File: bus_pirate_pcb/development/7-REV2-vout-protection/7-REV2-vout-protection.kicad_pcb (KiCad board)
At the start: 4 copper layers, 80 x 80.2 mm, 264 parts, among them J201 Conn_01x03, J202 TYPE-C-31-M-12, J301 Conn_01x10, J302 Conn_01x09, Q1 2N7002KT, Q2 2N7002KT, Q3 PMXB56EN, Q4 PMXB56EN, Q5 2N7002KT, Q6 2N7002KT, Q601 MMDT3906DW, Q602 BC2301T 2.8A, SW101 TS3425BA 098 2.5H 250gf, SW102 TS3315A 250gf 025, U1 RP2350B, U10 GS358-FR, U102 W25Q128JVSIQ, U105 MT29F2G01ABAGDWB-IT:G, U11 GS358-FR, U117 LM393BIDSGR, U12 GS358-FR, U13 GS358-FR, U14 SP3002-04JTG, U15 SP3002-04JTG, U16 SP3002-04JTG, U17 TLV75801PDRV, U2 AiP74LVC8T245QE24.TR, U301 AiP74LVC1T45GC363.TR, U302 AiP74LVC1T45GC363.TR, U303 AiP74LVC1T45GC363.TR, U304 AiP74LVC1T45GC363.TR, U305 AiP74LVC1T45GC363.TR, U306 AiP74LVC1T45GC363.TR, U307 AiP74LVC1T45GC363.TR, U308 AiP74LVC1T45GC363.TR, U4 XL9555QF24, U401 ME6211A33PG-N, U402 CD4067, U403 AP2127K-ADJ, U5 GS358-FR, U503 74HCT245BQ, U6 TCA6416ARTWR, U601 GS321A-TR, U602 GSV331-TR, U7 TCA6416ARTWR, U8 APS6404L-3SQR-ZR, U9 GS358-FR, Y101 ABM8-272-T3

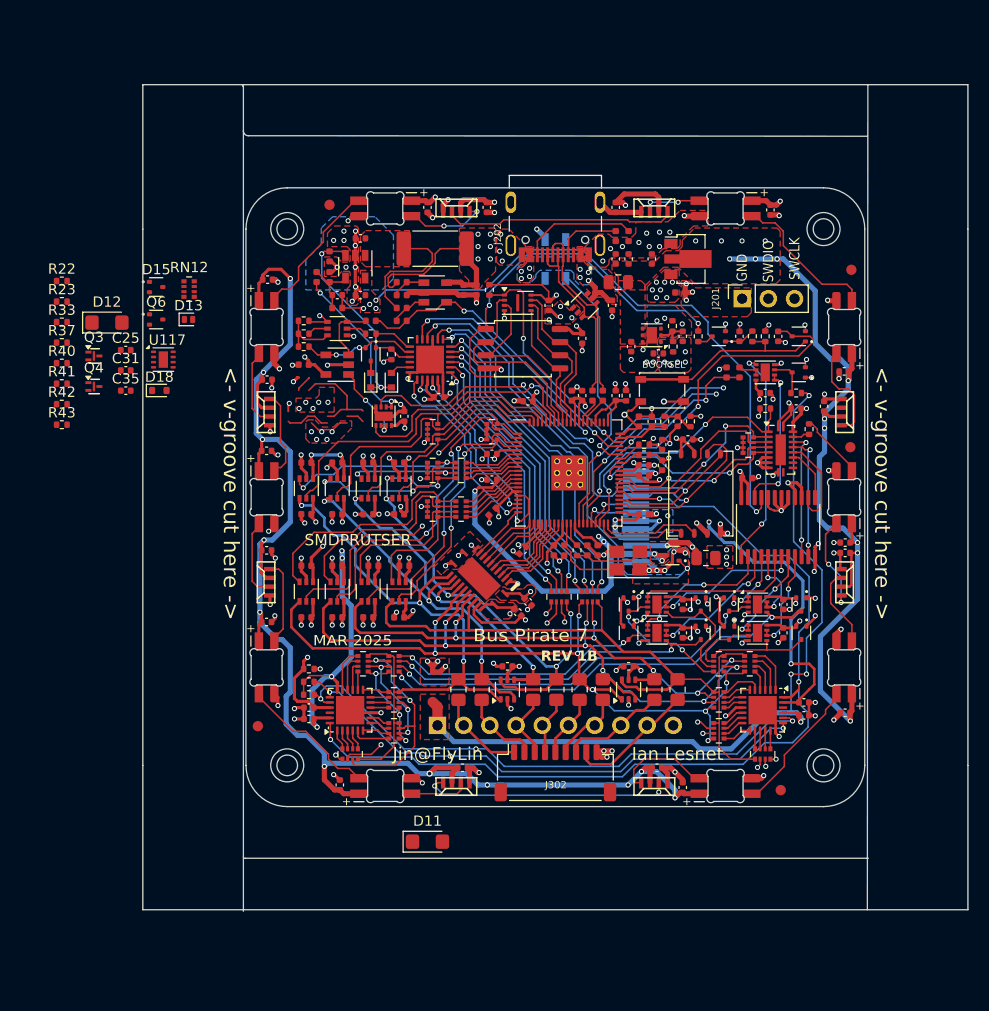
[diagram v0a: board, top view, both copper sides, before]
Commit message: BP 7R2 VOUT protection
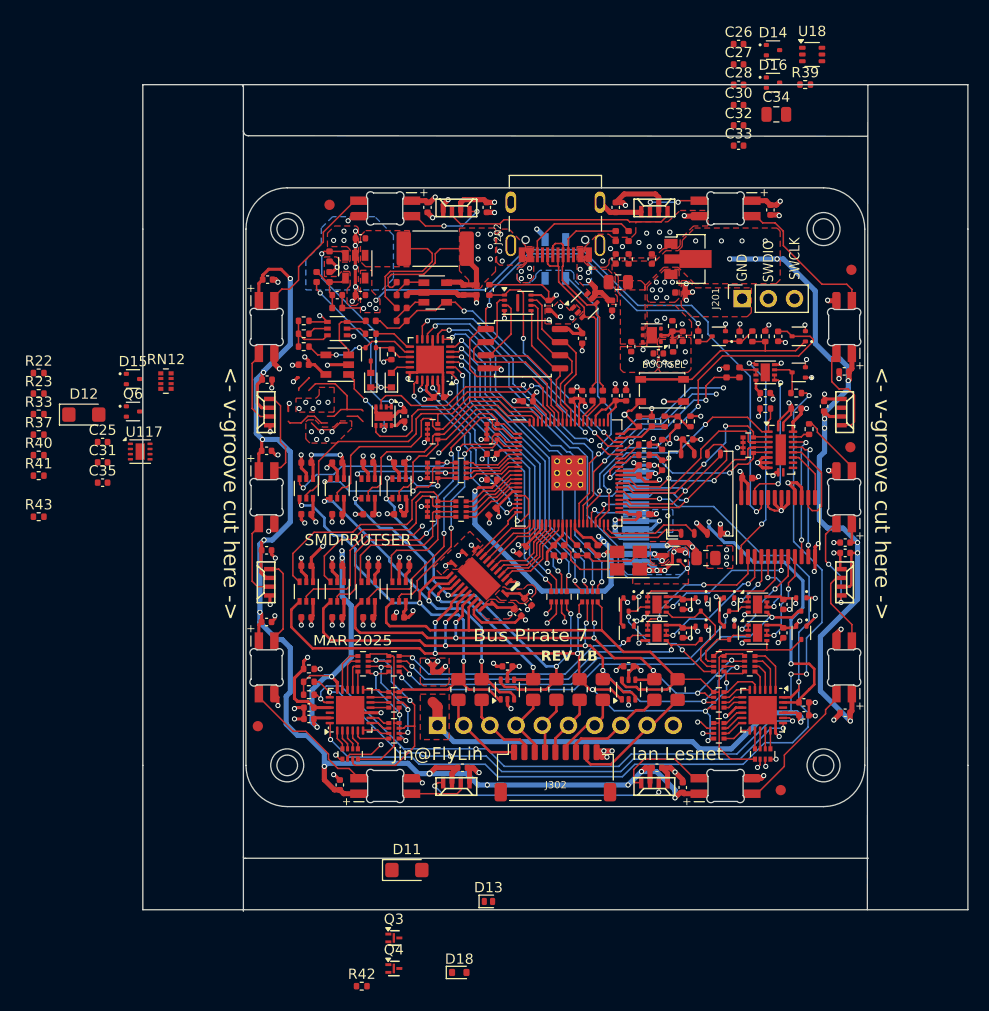
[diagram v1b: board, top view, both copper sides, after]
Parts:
- added C26: 120pF, Capacitor_SMD:C_0402_1005Metric, F.Cu at (147.7, 46.2)
- added C27: 10uF/6.3v, Capacitor_SMD:C_0402_1005Metric, F.Cu at (147.7, 48.1)
- added C28: 0.1uF, Capacitor_SMD:C_0402_1005Metric, F.Cu at (147.7, 50.1)
- added C30: 10uF/6.3v, Capacitor_SMD:C_0402_1005Metric, F.Cu at (147.7, 52.1)
- added C32: 0.1uF, Capacitor_SMD:C_0402_1005Metric, F.Cu at (147.7, 54.0)
- added C33: 10uF/6.3v, Capacitor_SMD:C_0402_1005Metric, F.Cu at (147.7, 56.0)
- added C34: 10uF/16v, Capacitor_SMD:C_0805_2012Metric, F.Cu at (151.3, 53.0)
- added D14: BAS40-04, Package_TO_SOT_SMD:SOT-523, F.Cu at (151.0, 46.8)
- added D16: BAS40-04, Package_TO_SOT_SMD:SOT-523, F.Cu at (151.0, 49.9)
- added R39: 180k, Resistor_SMD:R_0402_1005Metric, F.Cu at (154.1, 50.1)
- added U18: 74LVC2G14, Package_TO_SOT_SMD:SOT-363_SC-70-6, F.Cu at (154.8, 47.2)
- moved D13 63.5 mm to (123.4, 129.3)
- moved D18 63.5 mm to (120.6, 136.2)
- moved Q3 63.5 mm to (114.2, 132.8)
- moved Q4 63.5 mm to (114.2, 135.8)
- moved R42 63.5 mm to (111.1, 137.5)
- moved C25 9.20 mm to (86.0, 84.8)
- moved C31 9.20 mm to (86.0, 86.7)
- moved C35 9.20 mm to (86.0, 88.7)
- moved D12 9.20 mm to (84.2, 82.1)
- moved D15 9.20 mm to (88.9, 78.6)
- moved Q6 9.20 mm to (88.9, 81.8)
- moved R22 9.20 mm to (79.8, 78.1)
- moved R23 9.20 mm to (79.8, 80.0)
- moved R33 9.20 mm to (79.8, 82.0)
- moved R37 9.20 mm to (79.8, 84.0)
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
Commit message: 7R2 with vout protection
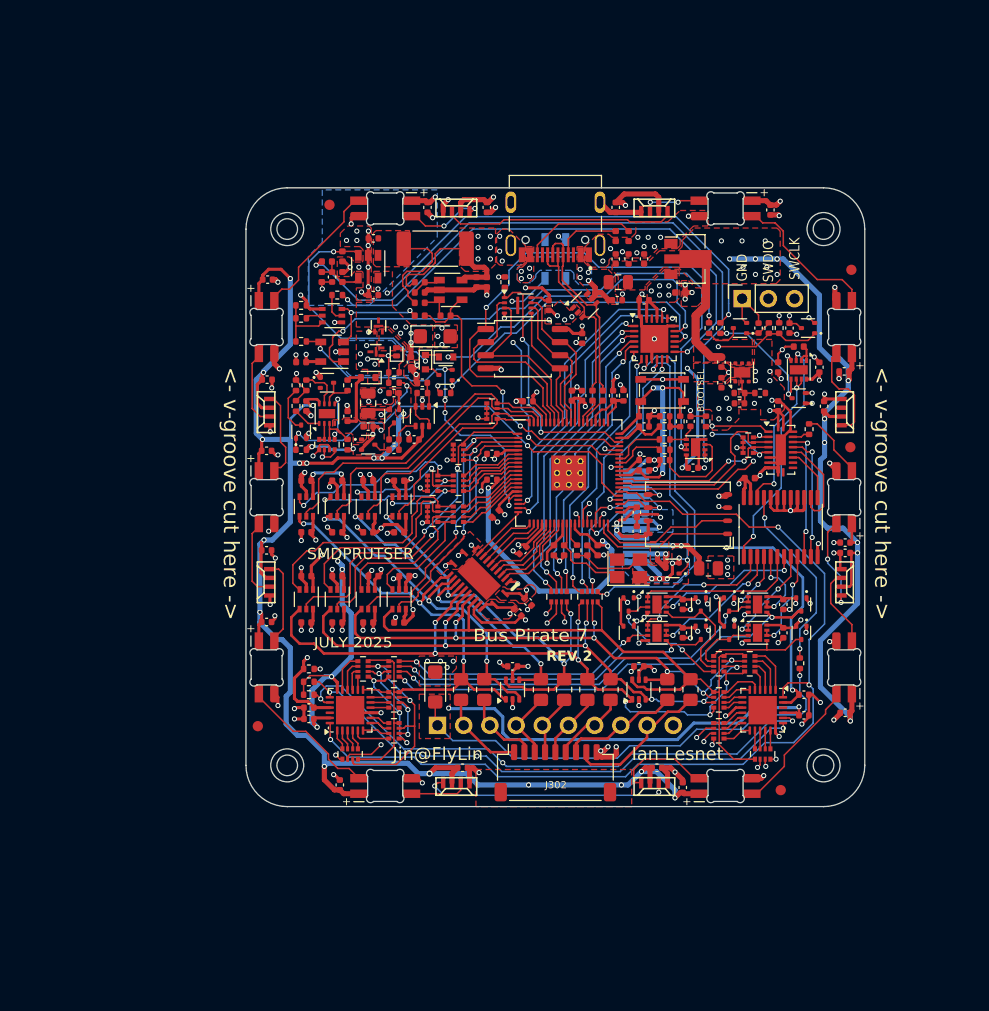
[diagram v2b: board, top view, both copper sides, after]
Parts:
- added R320: 0R, Resistor_SMD:R_0402_1005Metric, F.Cu at (153.6, 106.2)
- moved Q4 59.8 mm to (112.5, 76.0), turned to 180 degrees
- moved R42 59.6 mm to (114.2, 78.0), turned to 180 degrees
- moved Q3 59.4 mm to (112.8, 73.5), turned to 90 degrees
- moved D18 58.4 mm to (111.8, 78.5), turned to 180 degrees
- moved D13 54.0 mm to (114.5, 76.0), turned to 90 degrees
- moved D16 52.7 mm to (111.8, 85.0)
- moved U18 51.6 mm to (117.0, 82.2), turned to -90 degrees
- moved D14 51.1 mm to (114.2, 82.2), turned to -90 degrees
- moved C34 48.5 mm to (111.8, 81.0), turned to 90 degrees
- moved C28 48.0 mm to (114.2, 84.5), turned to 180 degrees
- moved R39 47.7 mm to (117.0, 80.0), turned to 180 degrees
- moved C27 46.2 mm to (114.2, 80.0), turned to 180 degrees
- moved C32 45.9 mm to (114.2, 85.5), turned to 180 degrees
- moved C30 45.2 mm to (116.2, 84.5), turned to 180 degrees
- moved C33 45.1 mm to (111.8, 83.2)
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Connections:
- C407 pad 1: VREG_OUT -> VREF_VOUT
- C408 pad 1: VREG_OUT -> VREF_VOUT
- D11 pad 2: VREF_VOUT -> VREF_VOUT_PROTECTED
- D18 pad 1: VREF_VOUT -> VREF_VOUT_PROTECTED
- D9 pad 3: Net-(U13A-+) -> Net-(U13B-+)
- J301 pad 1: VREF_VOUT -> VREF_VOUT_PROTECTED
- Q4 pad 3: VREF_VOUT -> VREF_VOUT_PROTECTED
- R319 pad 1: Net-(U13A-+) -> Net-(U13B-+)
- R404 pad 1: VREG_OUT -> VREF_VOUT
- R406 pad 1: Net-(U13B--) -> Net-(U13A--)
- RN12 pad 1: Net-(RN12A-R1.1) -> GND
- RN12 pad 2: GND -> VREF_VOUT
- RN12 pad 4: Net-(RN12D-R1.1) -> VREF_VOUT
- RN12 pad 5: VREF_VOUT -> Net-(RN12D-R1.8)
- RN12 pad 7: Net-(RN12A-R1.1) -> Net-(RN12A-R1.8)
- RN12 pad 8: VREF_VOUT -> Net-(RN12A-R1.8)
- SW102 pad 1: BUTTONS -> unconnected-(SW102-Pad1)
- SW102 pad 2: unconnected-(SW102-Pad2) -> GND
- SW102 pad 3: unconnected-(SW102-Pad3) -> BUTTONS
- SW102 pad 4: GND -> unconnected-(SW102-Pad4)
- U1 pad 45: unconnected-(U1-GPIO36-Pad45) -> ~{Activate_VOUT}
- U117 pad 2: Net-(RN12A-R1.1) -> Net-(RN12A-R1.8)
- U117 pad 5: Net-(RN12D-R1.1) -> Net-(RN12D-R1.8)
- U13 pad 1: MUX_VREF_VOUT -> Net-(U13A--)
- U13 pad 2: MUX_VREF_VOUT -> Net-(U13A--)
- U13 pad 6: Net-(U13B--) -> MUX_VREF_VOUT
- U13 pad 7: Net-(U13B--) -> MUX_VREF_VOUT
- U402 pad 1: Net-(U13B-+) -> Net-(U13A-+)
- U402 pad 21: VREG_OUT -> Net-(U402-I10)
- U403 pad 5: VREG_OUT -> VREF_VOUT
- U503 pad 21: (no net) -> GND
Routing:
- net VREF_VOUT_PROTECTED: track 0.00 -> 97.1 mm, vias 0 -> 6
- net VREG_OUT: track 73.9 -> 0.00 mm, vias 10 -> 0
- net CURRENT_ADJ: track 7.86 -> 59.9 mm
- net VREG_ADJ: track 16.2 -> 66.7 mm
- net CURRENT_RESET: track 3.80 -> 51.4 mm, vias 0 -> 2
- net +VUSB: track 302.1 -> 346.1 mm, vias 49 -> 58
- net ~{Activate_VOUT}: track 0.00 -> 39.1 mm, vias 0 -> 2
- net Net-(U5B-+): track 35.4 -> 3.03 mm, vias 3 -> 0
- net CURRENT_EN_OVERRIDE: track 2.02 -> 31.6 mm, vias 0 -> 2
- net CURRENT_EN: track 3.66 -> 31.3 mm, vias 0 -> 2
- net Net-(U5A-+): track 35.7 -> 9.52 mm, vias 3 -> 0
- net GND: track 237.4 -> 257.5 mm, vias 181 -> 186
- net Net-(D13-A1): track 0.00 -> 19.9 mm, vias 0 -> 3
- net DISPLAY_RESET: track 34.1 -> 14.7 mm
- net DISPLAY_BACKLIGHT: track 43.7 -> 24.4 mm
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- added copper zone on F.Cu, net +9V
- added copper zone on F.Cu, net -5V
- added copper zone on F.Cu, net Net-(D13-A2)
- added copper zone on B.Cu, net VREF_VOUT_PROTECTED
- added copper zone on F.Cu, net VREF_VOUT_PROTECTED
- added copper zone on In2.Cu, net VREF_VOUT_PROTECTED
- removed copper zone on F.Cu, net VREG_OUT
- removed copper zone on In2.Cu, net VREG_OUT
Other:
- board size 80 x 80.2 mm -> 60 x 60 mm
- board text added: "7R2"
- board text added: "JULY 2025"
- board text added: "REV 2"
- board text removed: "7R1B"
- board text removed: "MAR 2025"
- board text removed: "REV 1B"
